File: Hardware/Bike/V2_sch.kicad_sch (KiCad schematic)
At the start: 19 parts, among them U1 ESP32-WROOM-32

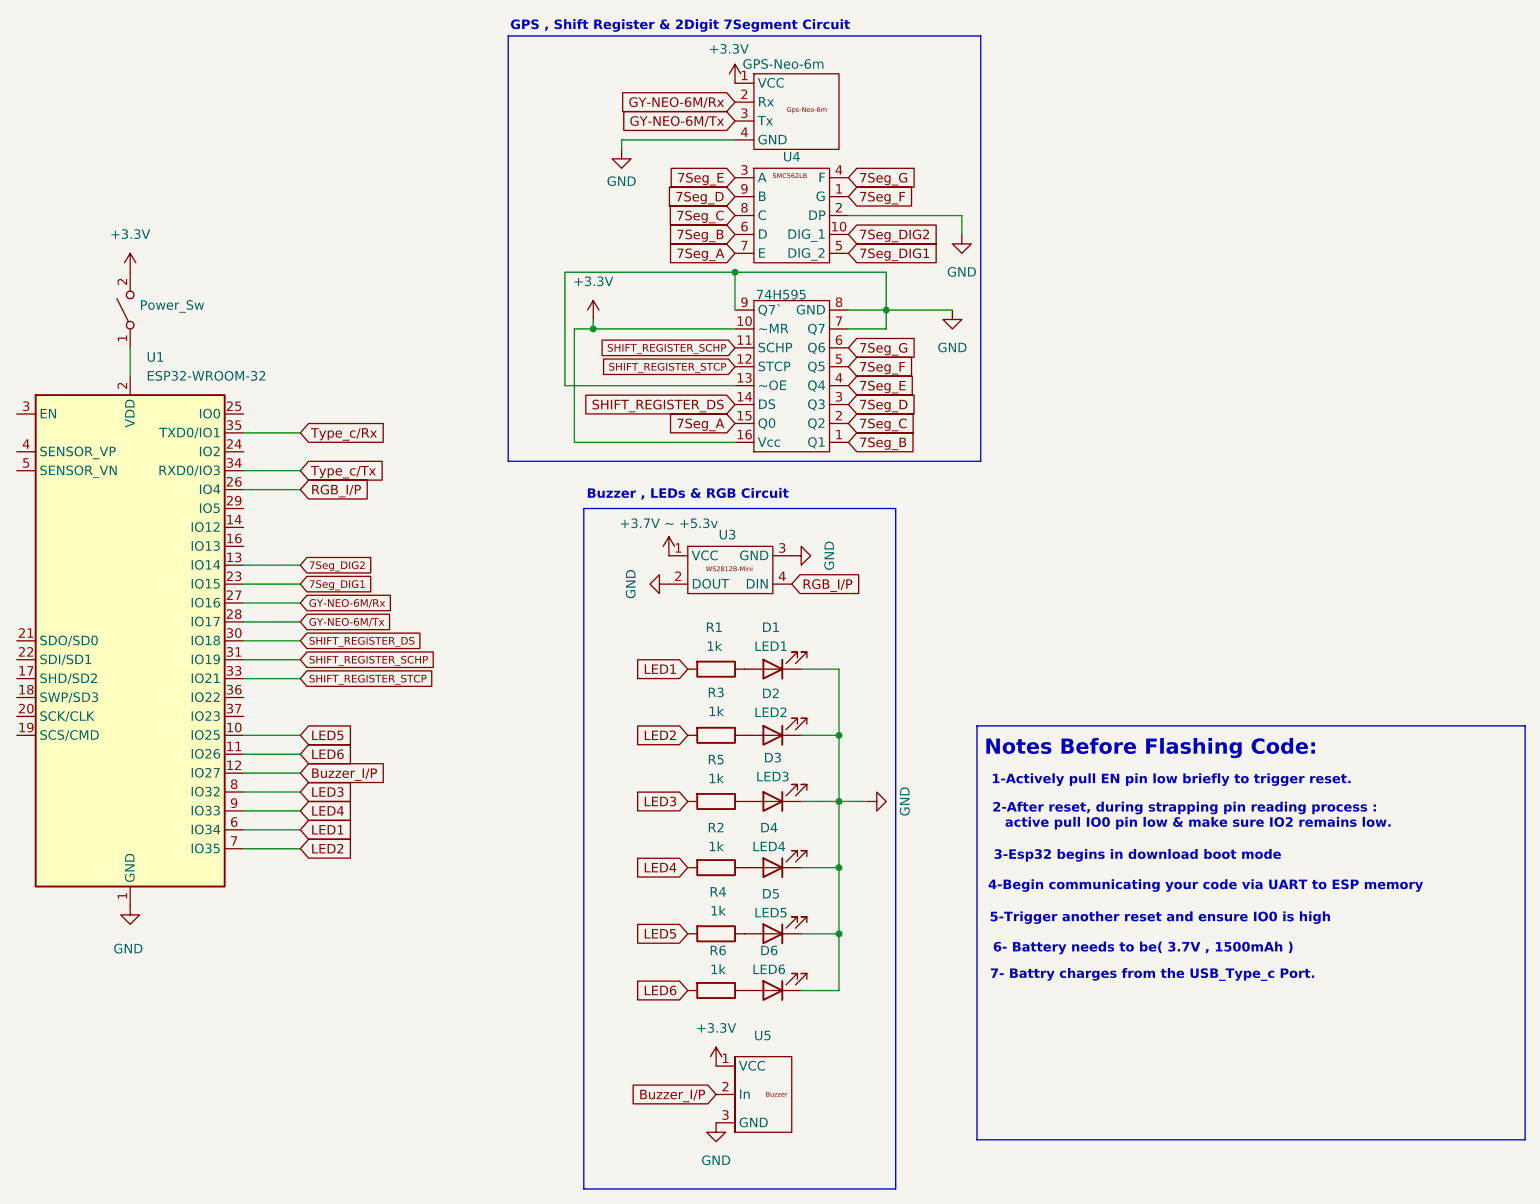
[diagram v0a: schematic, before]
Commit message: Added the 74H595 shift register to HW schematic and tested the 2digit 7segmments using the shitf register
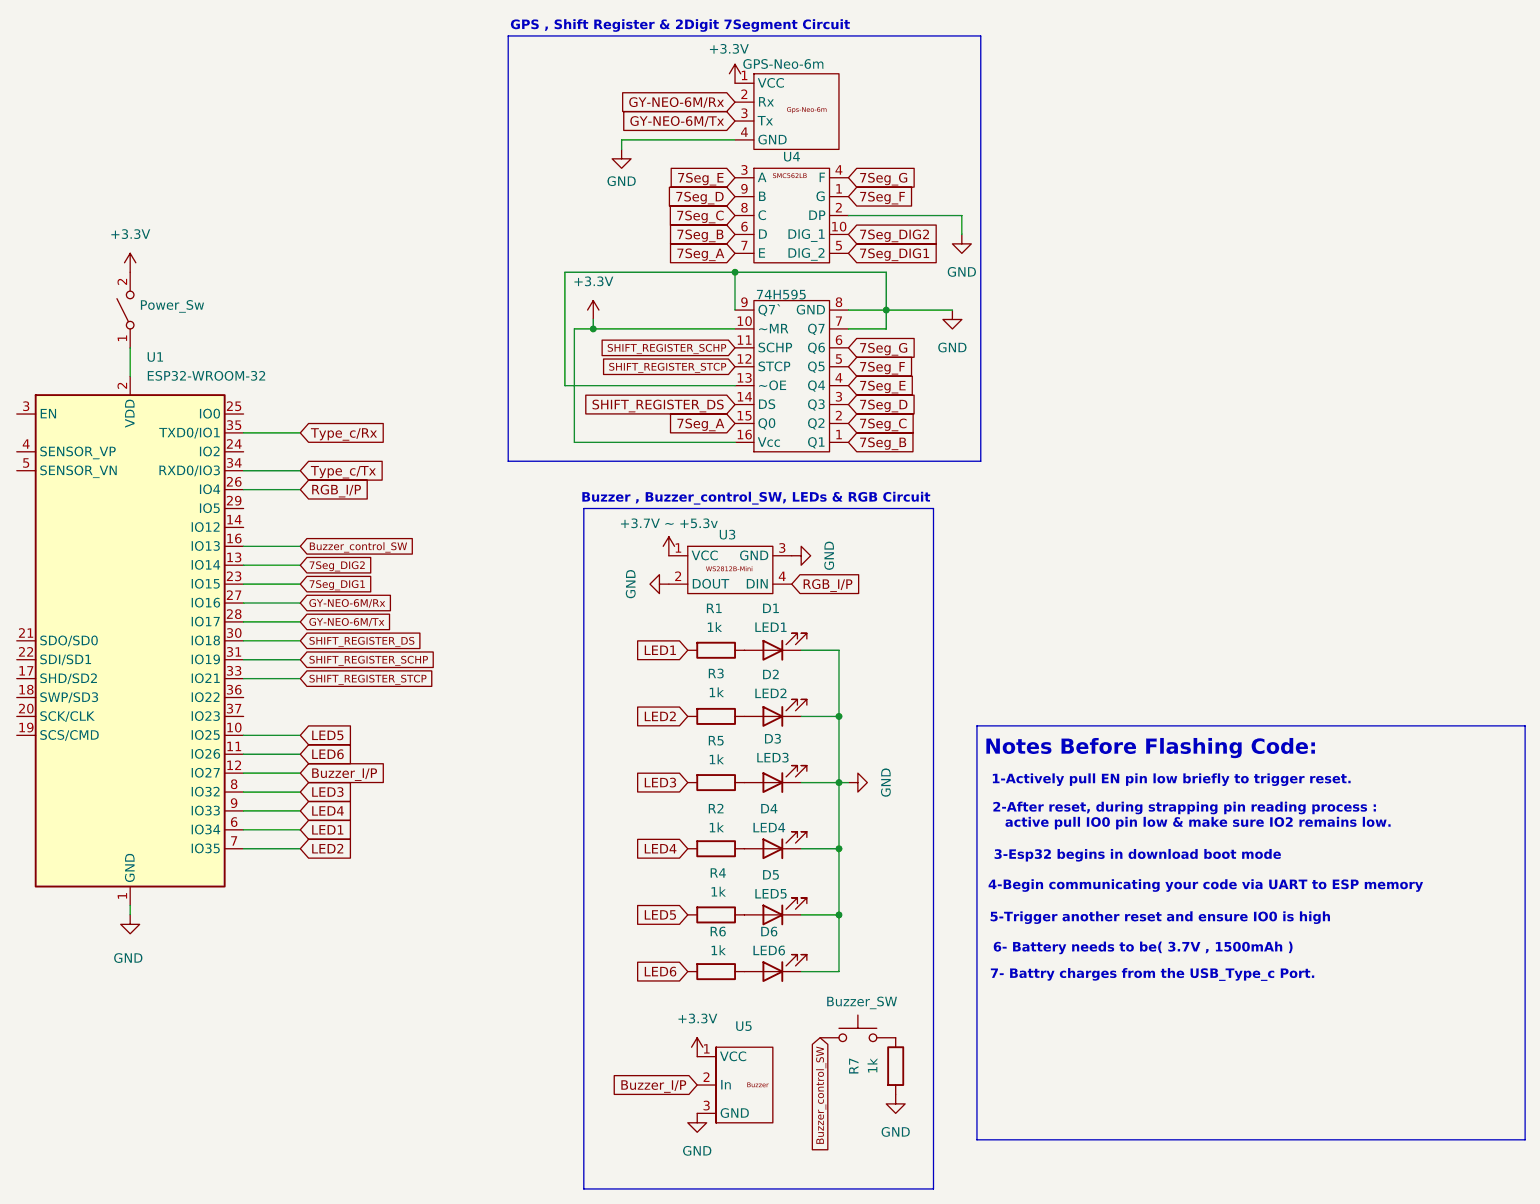
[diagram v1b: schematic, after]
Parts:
- added Buzzer_SW: ~, symbol Switch:SW_Push
- added R7: 1k, symbol Device:R
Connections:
- net GND: now also R7.2
- net Buzzer_control_SW: now reaches U1.16 (IO13)
- net Buzzer_control_SW: now also Buzzer_SW.1
- new net: Buzzer_SW.2, R7.1
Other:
- note added: "Buzzer , Buzzer_control_SW, LEDs & RGB Circuit"
- note removed: "Buzzer , LEDs & RGB Circuit"
- moved on the sheet: D1, D2, D3, D4, D5, D6, R1, R2, R3, R4, R5, R6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
